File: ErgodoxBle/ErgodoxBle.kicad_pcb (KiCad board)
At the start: 2 copper layers, 182.8 x 158.9 mm, 115 parts, among them SW0:10 SW0:3, SW0:11 SW0:2, SW0:12 SW0:1, SW0:7 SW0:6, SW0:8 SW0:5, SW0:9 SW0:4, SW1:10 SW1:3, SW1:11 SW1:2, SW1:12 SW1:1, SW1:13 SW1:0, SW1:9 SW1:4, SW2:10 SW2:3, SW2:11 SW2:2, SW2:12 SW2:1, SW2:13 SW2:0, SW2:7 SW2:6, SW2:8 SW2:5, SW2:9 SW2:4, SW3:10 SW3:3, SW3:11 SW3:2, SW3:12 SW3:1, SW3:13 SW3:0, SW3:8 SW3:5, SW3:9 SW3:4, SW4:10 SW4:3, SW4:11 SW4:2, SW4:12 SW4:1, SW4:13 SW4:0, SW4:7 SW4:6, SW4:8 SW4:5, SW4:9 SW4:4, SW5:10 SW5:3, SW5:11 SW5:2, SW5:12 SW5:1, SW5:13 SW5:0, SW5:7 SW5:6, SW5:8 SW5:5, SW5:9 SW5:4

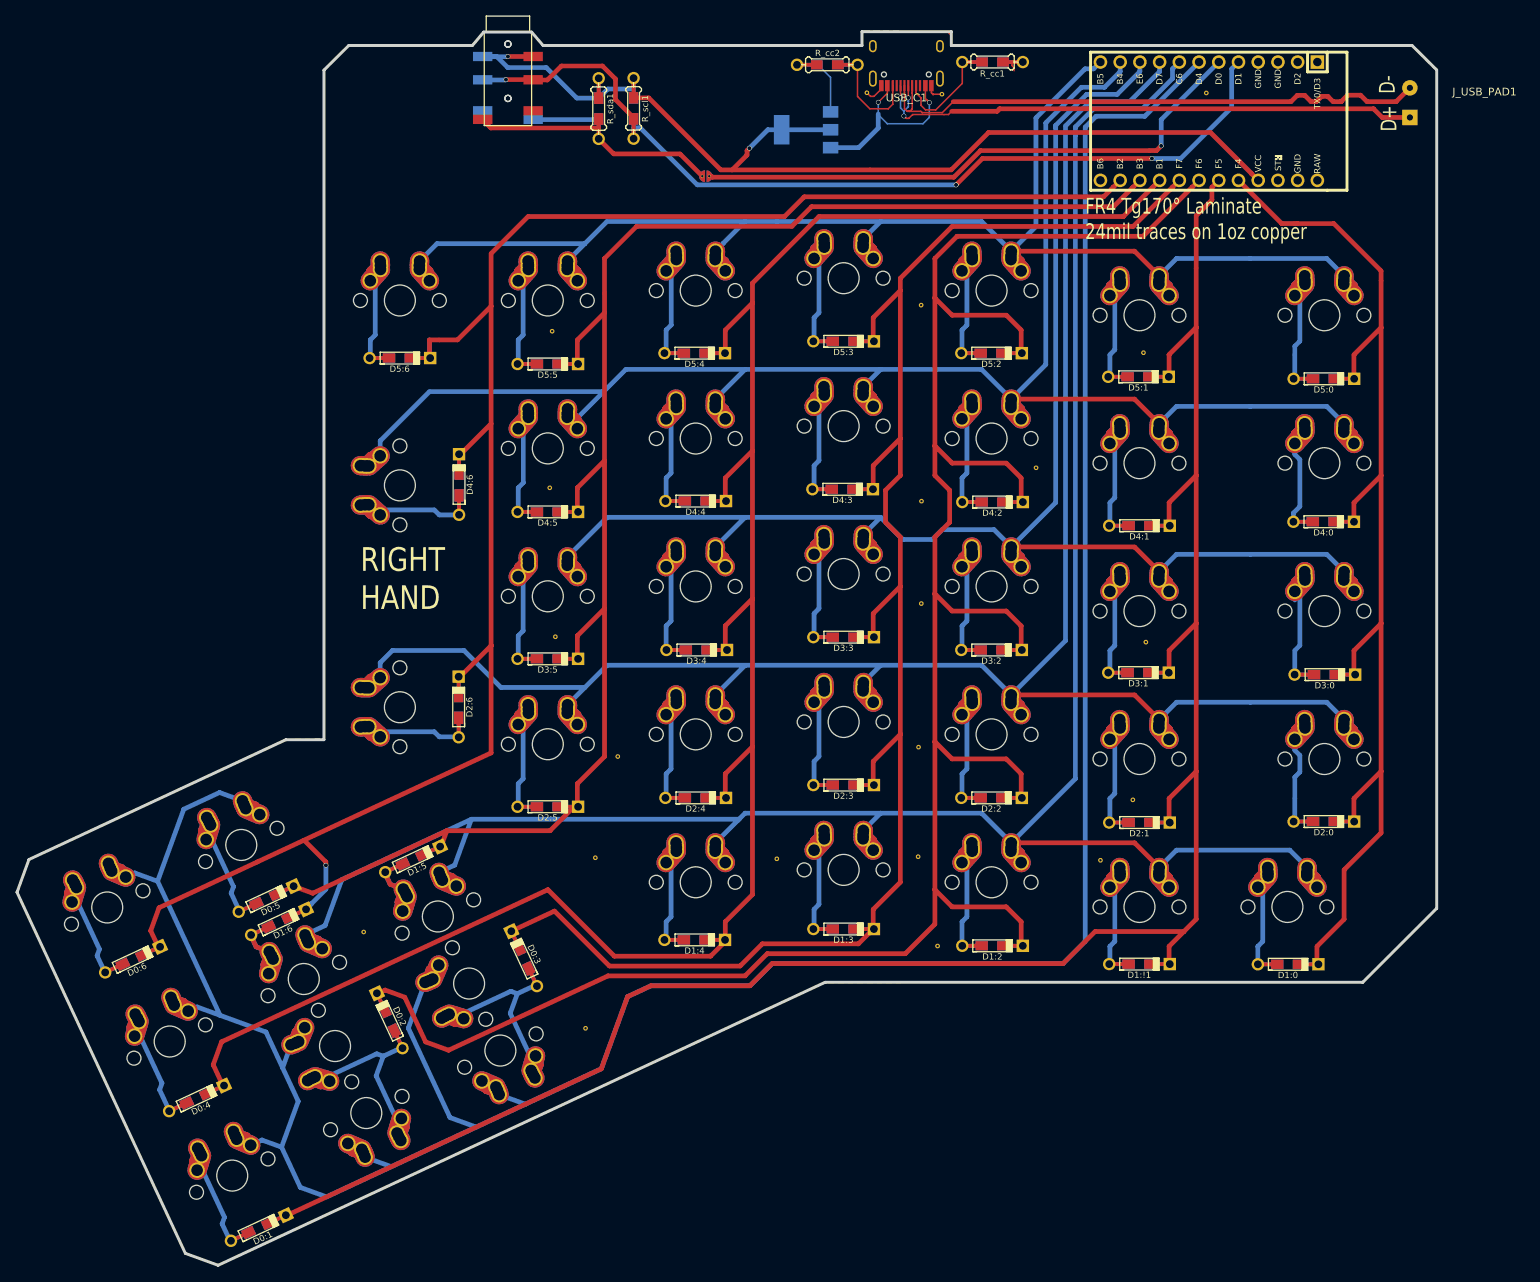
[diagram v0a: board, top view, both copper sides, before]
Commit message: update pcb, removed unwanted i2c wire, will go only serial over sda
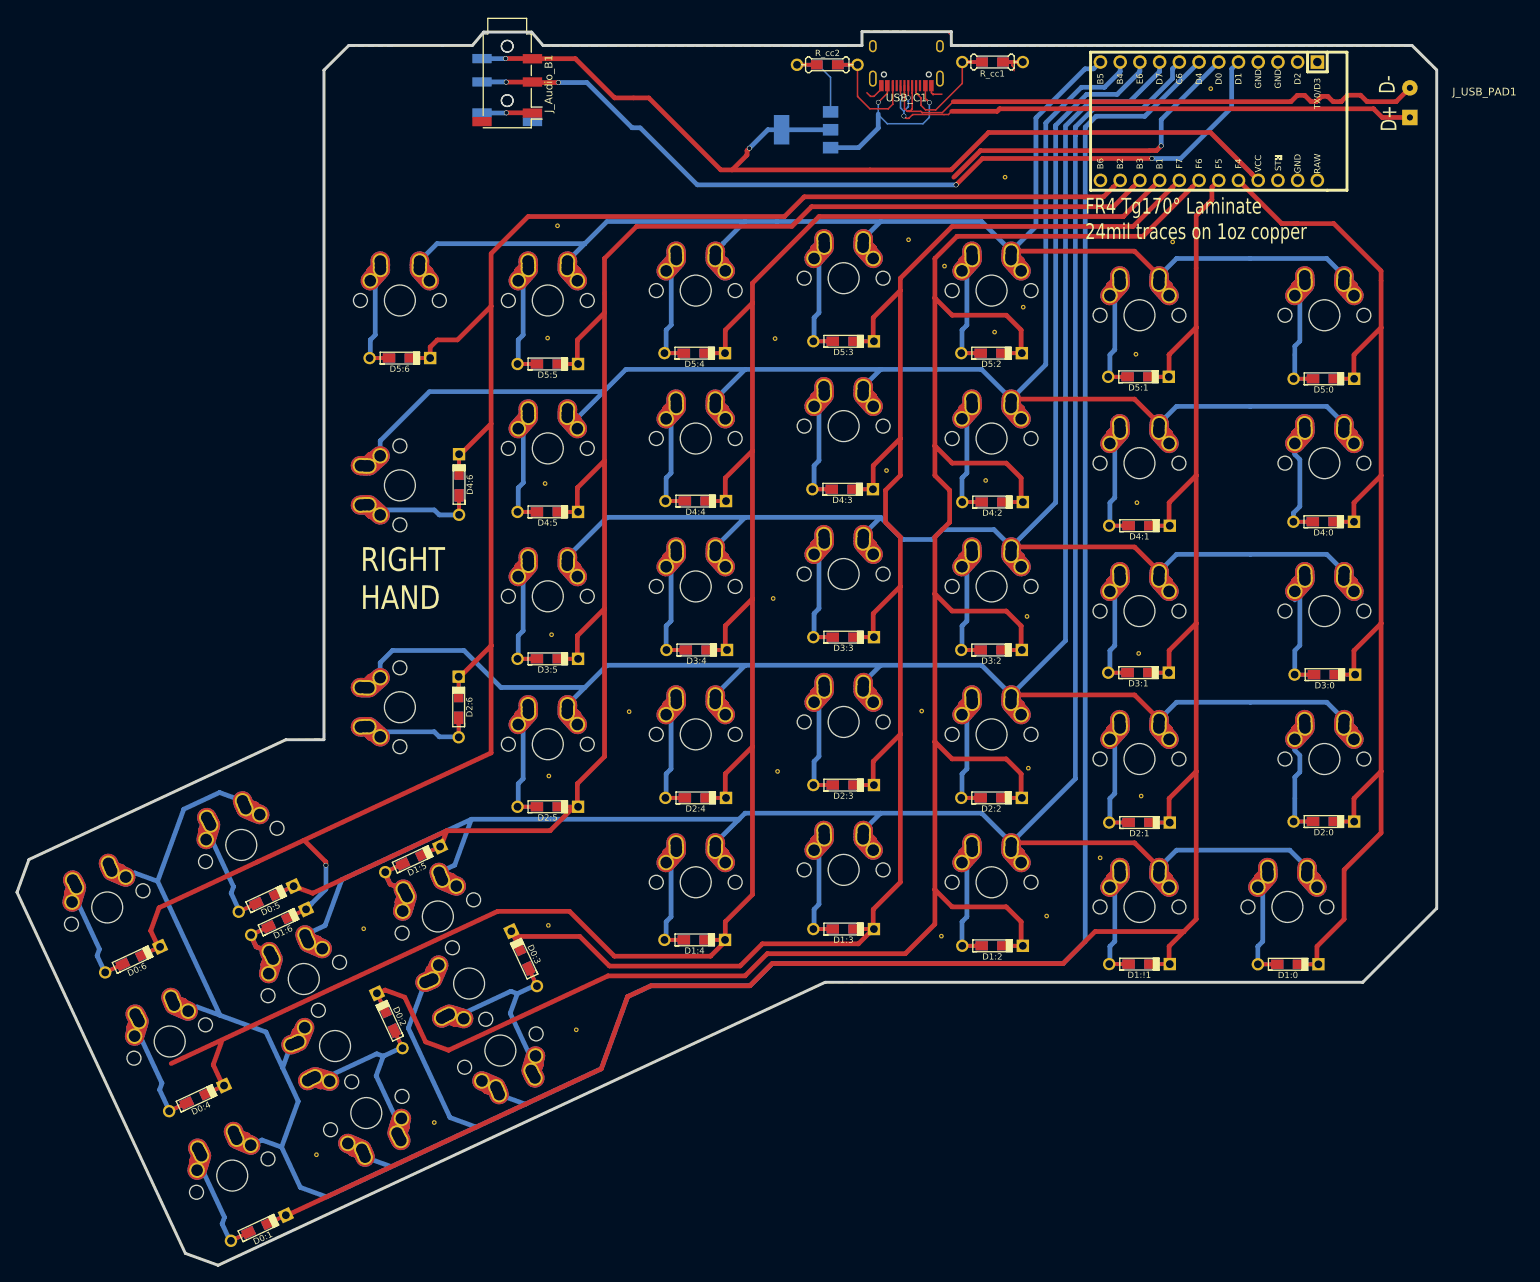
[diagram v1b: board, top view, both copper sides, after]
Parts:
- removed JP1: SolderJumper_2_Open, Keebio-Parts:solder_jumper
- removed the REF** at (142.2, 38.5)
- removed the REF** at (166.8, 129.4)
- removed the REF** at (168.5, 109.1)
- removed the REF** at (154.3, 86.6)
- removed the REF** at (100.5, 123.8)
- removed the REF** at (139.2, 122.6)
- removed the REF** at (139.5, 104.1)
- removed the REF** at (139.6, 90.9)
- removed the REF** at (168.2, 71.8)
- removed the REF** at (92.0, 69.1)
- removed the REF** at (139.5, 65.7)
- removed the REF** at (132.5, 38.3)
- removed the REF** at (139.1, 136.7)
- removed the REF** at (120.9, 137.0)
- removed the REF** at (97.6, 136.9)
- removed the REF** at (176.2, 38.4)
- removed the REF** at (91.7, 89.2)
- removed the REF** at (92.4, 108.4)
- removed the REF** at (67.7, 146.4)
- removed the REF** at (96.3, 158.8)
- removed the REF** at (141.6, 148.2)
- removed the REF** at (162.6, 137.2)
- removed R_scl1, R_sda1: 47k, Keebio-Parts:Resistor-Hybrid
- added REF**: via-0.6mm, usbc_footprint:via-0.6mm, F.Cu at (176.8, 37.8)
- added REF**: via-0.6mm, usbc_footprint:via-0.6mm, F.Cu at (121.0, 125.7)
- added REF**: via-0.6mm, usbc_footprint:via-0.6mm, F.Cu at (153.2, 105.8)
- added REF**: via-0.6mm, usbc_footprint:via-0.6mm, F.Cu at (76.8, 171.0)
- added REF**: via-0.6mm, usbc_footprint:via-0.6mm, F.Cu at (167.3, 91.1)
- added REF**: via-0.6mm, usbc_footprint:via-0.6mm, F.Cu at (67.7, 146.0)
- added REF**: via-0.6mm, usbc_footprint:via-0.6mm, F.Cu at (91.9, 108.1)
- added REF**: via-0.6mm, usbc_footprint:via-0.6mm, F.Cu at (153.3, 125.3)
- added REF**: via-0.6mm, usbc_footprint:via-0.6mm, F.Cu at (155.7, 144.4)
- added REF**: via-0.6mm, usbc_footprint:via-0.6mm, F.Cu at (120.7, 70.0)
- added REF**: via-0.6mm, usbc_footprint:via-0.6mm, F.Cu at (167.9, 128.9)
- added REF**: via-0.6mm, usbc_footprint:via-0.6mm, F.Cu at (171.9, 57.6)
- added REF**: via-0.6mm, usbc_footprint:via-0.6mm, F.Cu at (139.6, 118.0)
- added REF**: via-0.6mm, usbc_footprint:via-0.6mm, F.Cu at (149.0, 69.2)
- added REF**: via-0.6mm, usbc_footprint:via-0.6mm, F.Cu at (120.5, 103.5)
- added REF**: via-0.6mm, usbc_footprint:via-0.6mm, F.Cu at (137.9, 57.3)
- added REF**: via-0.6mm, usbc_footprint:via-0.6mm, F.Cu at (142.1, 147.0)
- added REF**: via-0.6mm, usbc_footprint:via-0.6mm, F.Cu at (167.5, 110.6)
- added REF**: via-0.6mm, usbc_footprint:via-0.6mm, F.Cu at (92.7, 55.5)
- added REF**: via-0.6mm, usbc_footprint:via-0.6mm, F.Cu at (147.8, 88.3)
- added REF**: via-0.6mm, usbc_footprint:via-0.6mm, F.Cu at (167.2, 72.0)
- added REF**: via-0.6mm, usbc_footprint:via-0.6mm, F.Cu at (91.4, 69.9)
- added REF**: via-0.6mm, usbc_footprint:via-0.6mm, F.Cu at (150.3, 49.2)
- added REF**: via-0.6mm, usbc_footprint:via-0.6mm, F.Cu at (101.9, 118.1)
- added REF**: via-0.6mm, usbc_footprint:via-0.6mm, F.Cu at (91.6, 126.3)
- added REF**: via-0.6mm, usbc_footprint:via-0.6mm, F.Cu at (152.7, 66.0)
- added REF**: via-0.6mm, usbc_footprint:via-0.6mm, F.Cu at (91.1, 88.7)
- added REF**: via-0.6mm, usbc_footprint:via-0.6mm, F.Cu at (135.1, 87.0)
- added REF**: via-0.6mm, usbc_footprint:via-0.6mm, F.Cu at (142.5, 60.7)
- added REF**: via-0.6mm, usbc_footprint:via-0.6mm, F.Cu at (61.6, 175.1)
- added REF**: via-0.6mm, usbc_footprint:via-0.6mm, F.Cu at (91.5, 145.6)
- added REF**: via-0.6mm, usbc_footprint:via-0.6mm, F.Cu at (162.6, 136.9)
- added REF**: via-0.6mm, usbc_footprint:via-0.6mm, F.Cu at (95.1, 159.0)
- J_Audio_B1, J_Audio_F1: footprint Keebio-Parts:TRRS-PJ-320D -> Connector_Audio:Jack_3.5mm_PJ320D_Horizontal
- moved J_Audio_B1 6.66 mm to (86.2, 37.1), turned to 270 degrees
- moved J_Audio_F1 6.65 mm to (86.2, 37.1), turned to 270 degrees
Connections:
- proMicro1 pad 6: /sdaM -> Net-(proMicro1-Pad6)
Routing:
- net /sdaM: track 73.8 -> 0.00 mm, vias 1 -> 0
- net Net-(proMicro1-Pad6): track 0.00 -> 42.2 mm, vias 0 -> 1
- net /sda: track 39.2 -> 0.00 mm
- net /Vcc: track 132.7 -> 125.6 mm
- net GND: track 13.4 -> 19.9 mm, vias 0 -> 1
- net /COL4: track 253.3 -> 258.6 mm
- net /COL6: track 240.4 -> 237.0 mm
- net /scl: track 115.1 -> 112.4 mm, vias 3 -> 4
- net /COL10: track 210.1 -> 208.3 mm

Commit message: Added pad for CR2032 module for bluemicro
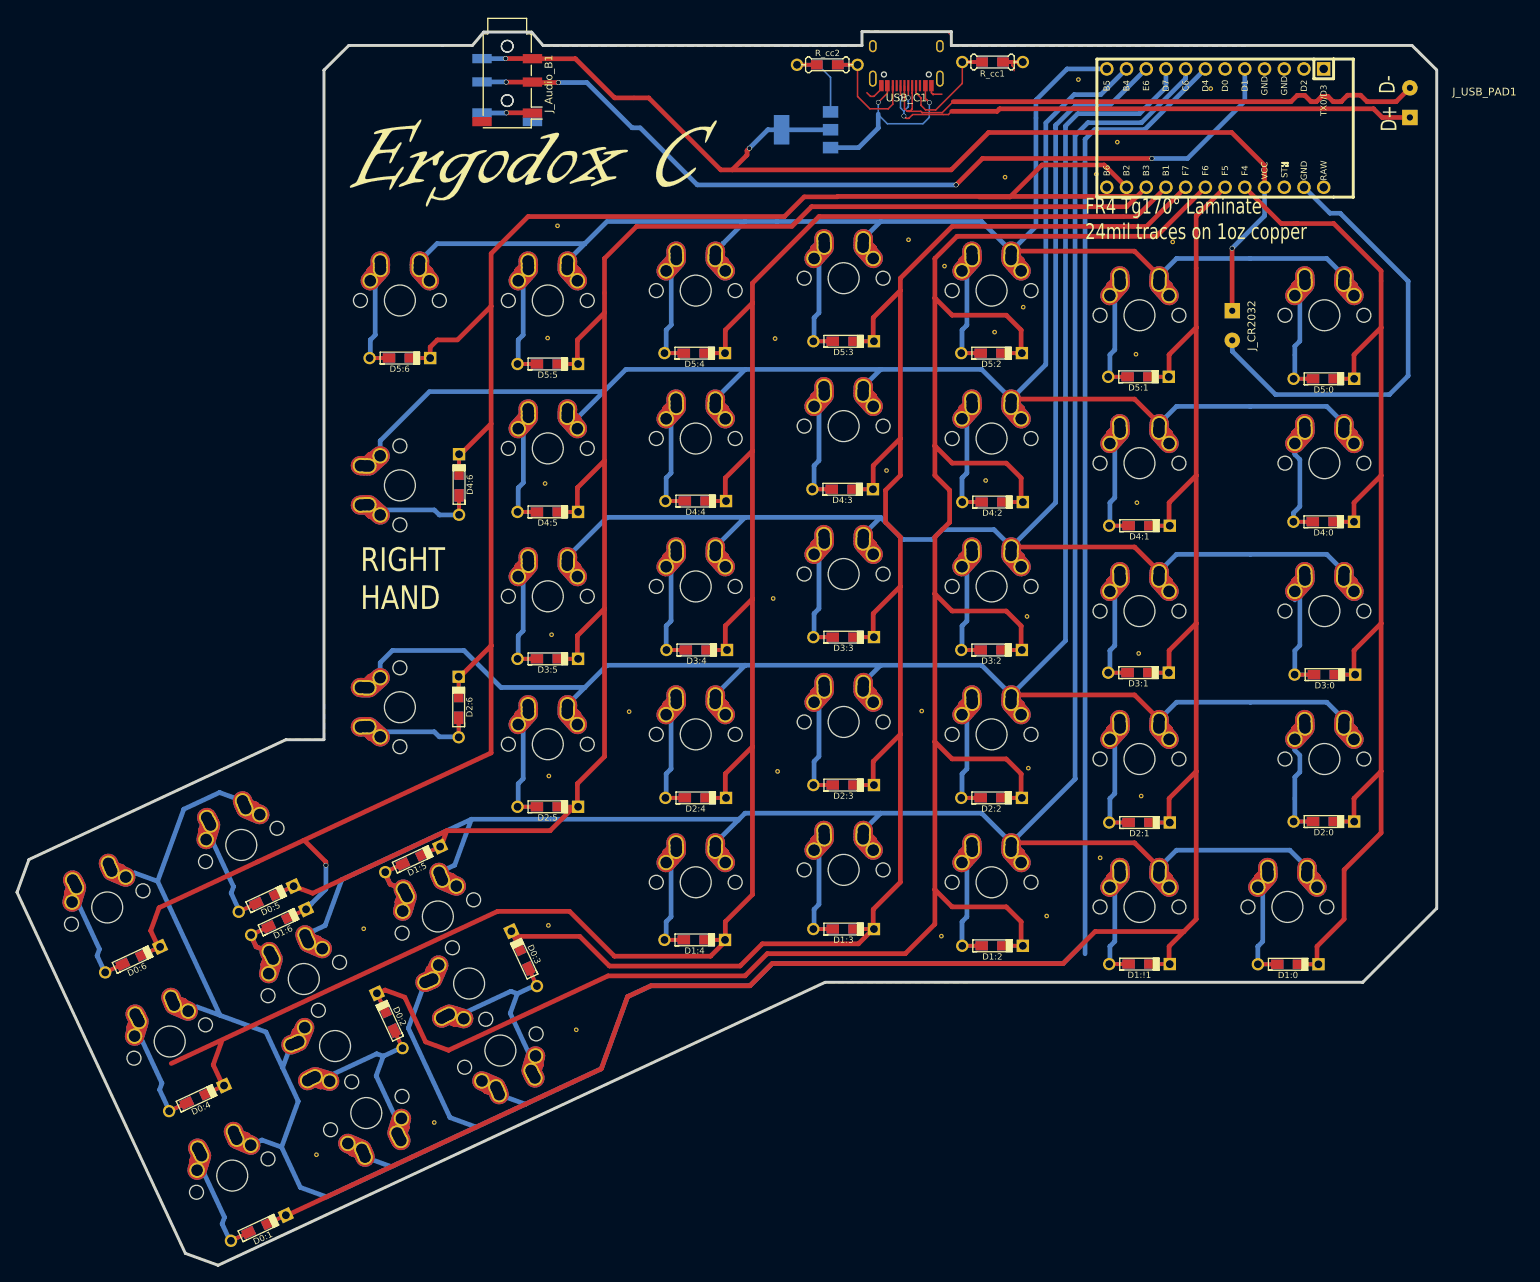
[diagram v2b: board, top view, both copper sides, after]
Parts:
- added G***: LOGO, usbc_footprint:Ergodox-V, F.Cu at (90.2, 47.7)
- added G***: LOGO, usbc_footprint:Ergodox-V_Back, F.Cu at (89.6, 47.3)
- added J_CR2032: Conn_01x02_Female, Connector_Wire:SolderWirePad_1x02_P3.81mm_Drill0.8mm, F.Cu at (179.6, 66.4)
- added REF**: via-0.6mm, usbc_footprint:via-0.6mm, F.Cu at (162.1, 48.8)
- added REF**: via-0.6mm, usbc_footprint:via-0.6mm, F.Cu at (159.8, 36.7)
- added REF**: via-0.6mm, usbc_footprint:via-0.6mm, F.Cu at (164.8, 44.7)
- moved proMicro1 1.20 mm to (177.4, 42.9)
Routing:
- net GND: track 19.9 -> 77.9 mm
- net Net-(proMicro1-Pad6): track 42.2 -> 0.00 mm, vias 1 -> 0
- net /COL6: track 237.0 -> 260.2 mm
- net /Vcc: track 125.6 -> 146.1 mm, vias 2 -> 3
- net /ROW5: track 206.7 -> 208.5 mm
- net /COL0: track 146.1 -> 144.9 mm
- net /ROW0: track 397.5 -> 398.6 mm
- net /ROW2: track 281.7 -> 282.8 mm
- net /COL1: track 263.6 -> 263.1 mm

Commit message: v 1.3, almost the final version
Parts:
- removed J_USB_PAD1: Conn_01x02_Female, Connector_Wire:SolderWirePad_1x02_P3.81mm_Drill0.8mm
- removed the REF** at (162.1, 48.8)
- removed the REF** at (159.8, 36.7)
- removed U_VR_IC1: AMS1117-3.3, Package_TO_SOT_SMD:SOT-223-3_TabPin2
- added D_RAW1: D, Keebio-Parts:Diode-dual, F.Cu at (119.8, 42.2)
- added D_USB_HEADER1: D, Keebio-Parts:Diode-dual, F.Cu at (112.7, 40.6)
- added J_usb_break1: Conn_01x04_Female, Connector_Wire:SolderWirePad_1x04_P3.81mm_Drill1mm, F.Cu at (202.6, 48.0)
- added REF**: via-0.6mm, usbc_footprint:via-0.6mm, F.Cu at (170.2, 36.8)
- added REF**: via-0.6mm, usbc_footprint:via-0.6mm, F.Cu at (177.0, 47.4)
- added REF**: via-0.6mm, usbc_footprint:via-0.6mm, F.Cu at (162.1, 48.5)
- added REF**: VIA-0.6mm, Keebio-Parts:VIA-0.6mm, F.Cu at (180.4, 54.2)
- added REF**: via-0.6mm, usbc_footprint:via-0.6mm, F.Cu at (159.8, 36.9)
- added REF**: VIA-0.6mm, Keebio-Parts:VIA-0.6mm, F.Cu at (116.1, 46.6)
- added REF**: VIA-0.6mm, Keebio-Parts:VIA-0.6mm, F.Cu at (190.7, 43.0)
- added REF**: VIA-0.6mm, Keebio-Parts:VIA-0.6mm, F.Cu at (144.6, 41.3)
- added U_ESD1: USBLC6-2SC6, Package_TO_SOT_SMD:SOT-23-6, F.Cu at (147.3, 39.6)
- moved REF** 19.3 mm to (196.0, 36.2)
- moved REF** 14.2 mm to (150.5, 44.8)
- moved proMicro1 2.73 mm to (179.8, 41.7)
- moved R_cc1 0.76 mm to (148.7, 35.1)
- moved REF** 0.59 mm to (172.4, 57.9)
- moved USB_C1 0.52 mm to (137.6, 29.2)
- moved REF** 0.39 mm to (153.6, 125.1)
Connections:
- net /D+ renamed /D_IN+
- net /D- renamed /D_IN-
- REF** pad 1: (no net) -> GND
- USB_C1 pad 1: GND -> /GND_USB
- USB_C1 pad 12: GND -> /GND_USB
- proMicro1 pad 23: GND -> /GND_USB
- proMicro1 pad 24: Net-(proMicro1-Pad24) -> /VccRaw
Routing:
- net /GND_USB: track 0.00 -> 108.8 mm, vias 0 -> 5
- net /VUSB: track 0.00 -> 93.6 mm
- net /VccRaw: track 0.00 -> 78.0 mm, vias 0 -> 1
- net /D_IN-: track 75.8 -> 17.2 mm
- net /D_IN+: track 73.9 -> 17.1 mm
- net /D-: track 0.00 -> 56.3 mm
- net /D+: track 0.00 -> 55.9 mm
- net /VccR: track 25.3 -> 62.5 mm, vias 2 -> 4
- net /Vcc: track 146.1 -> 126.9 mm, vias 3 -> 5
- net GND: track 77.9 -> 62.5 mm, vias 1 -> 3
- net /COL6: track 260.2 -> 245.3 mm
- net /ROW0: track 398.6 -> 401.6 mm
- net /COL11: track 283.7 -> 286.7 mm
- net /ROW4: track 242.4 -> 245.4 mm
- net /ROW3: track 224.7 -> 227.6 mm
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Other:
- board text added: "BLUEMICRO ONLY"
- board text added: "PROTONC ONLY"
- board text added: "V1.3"

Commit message: final version before hardware testing
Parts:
- added USB_C2: HRO-TYPE-C-31-M-12, usbc_footprint:HRO-TYPE-C-31-M-12, B.Cu at (137.6, 29.2)
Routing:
- net /D_IN-: track 17.2 -> 25.8 mm, vias 0 -> 1
- net /VccR: track 62.5 -> 68.5 mm
- net /CC1: track 11.8 -> 17.0 mm, vias 0 -> 1
- net /GND_USB: track 108.8 -> 113.4 mm
- net /D_IN+: track 17.1 -> 21.4 mm
- net /VUSB: track 93.6 -> 94.7 mm

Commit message: minor changes
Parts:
- removed D_RAW1, D_USB_HEADER1: D, Keebio-Parts:Diode-dual
- removed the REF** at (144.6, 41.3)
- added REF**: VIA-0.6mm, Keebio-Parts:VIA-0.6mm, F.Cu at (148.5, 60.6)
- added REF**: VIA-0.6mm, Keebio-Parts:VIA-0.6mm, F.Cu at (91.4, 61.6)
- added REF**: VIA-0.6mm, Keebio-Parts:VIA-0.6mm, F.Cu at (129.5, 58.7)
- added REF**: VIA-0.6mm, Keebio-Parts:VIA-0.6mm, F.Cu at (129.4, 78.0)
- added REF**: VIA-0.6mm, Keebio-Parts:VIA-0.6mm, F.Cu at (91.4, 80.9)
- added REF**: VIA-0.6mm, Keebio-Parts:VIA-0.6mm, F.Cu at (91.4, 119.0)
- added REF**: VIA-0.6mm, Keebio-Parts:VIA-0.6mm, F.Cu at (129.5, 135.2)
- added REF**: VIA-0.6mm, Keebio-Parts:VIA-0.6mm, F.Cu at (129.6, 116.1)
- added REF**: VIA-0.6mm, Keebio-Parts:VIA-0.6mm, F.Cu at (129.6, 97.1)
- added REF**: VIA-0.6mm, Keebio-Parts:VIA-0.6mm, F.Cu at (148.6, 98.7)
- added REF**: VIA-0.6mm, Keebio-Parts:VIA-0.6mm, F.Cu at (186.7, 139.9)
- added REF**: VIA-0.6mm, Keebio-Parts:VIA-0.6mm, F.Cu at (191.4, 120.8)
- added REF**: VIA-0.6mm, Keebio-Parts:VIA-0.6mm, F.Cu at (191.4, 101.8)
- added REF**: VIA-0.6mm, Keebio-Parts:VIA-0.6mm, F.Cu at (191.4, 82.7)
- added REF**: VIA-0.6mm, Keebio-Parts:VIA-0.6mm, F.Cu at (191.4, 63.5)
- added REF**: VIA-0.6mm, Keebio-Parts:VIA-0.6mm, F.Cu at (83.8, 32.2)
- added REF**: VIA-0.6mm, Keebio-Parts:VIA-0.6mm, F.Cu at (88.4, 32.1)
- added REF**: VIA-0.6mm, Keebio-Parts:VIA-0.6mm, F.Cu at (170.9, 144.5)
- added REF**: VIA-0.6mm, Keebio-Parts:VIA-0.6mm, F.Cu at (154.4, 60.1)
- moved REF** 0.65 mm to (153.7, 105.5)
- moved REF** 0.54 mm to (150.5, 44.2)
- moved REF** 0.49 mm to (177.1, 46.9)
- moved REF** 0.18 mm to (142.7, 60.5)
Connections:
- USB_C1 pad 11: /VccR -> /VUSB
- USB_C1 pad 2: /VccR -> /VUSB
- USB_C2 pad 11: /VccR -> /VUSB
- USB_C2 pad 2: /VccR -> /VUSB
- U_ESD1 pad 5: /VccR -> /VUSB
- proMicro1 pad 23: /GND_USB -> Net-(proMicro1-Pad23)
- proMicro1 pad 24: /VccRaw -> Net-(proMicro1-Pad24)
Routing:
- net /VccRaw: track 78.0 -> 0.00 mm, vias 1 -> 0
- net /VccR: track 68.5 -> 0.00 mm, vias 4 -> 0
- net /GND_USB: track 113.4 -> 98.5 mm
- net GND: track 62.5 -> 58.0 mm
- net /VUSB: track 94.7 -> 91.3 mm, vias 0 -> 5
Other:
- board text removed: "BLUEMICRO ONLY"
- board text removed: "PROTONC ONLY"
